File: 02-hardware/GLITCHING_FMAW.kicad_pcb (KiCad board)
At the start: 4 copper layers, 49 x 49 mm, 72 parts, among them J1 USB_C_Receptacle_USB2.0_16P, J2 AIN, J3 GLITCH, J4 ANA1, J5 ANA2, J6 ANA3, J7 GND, Q2 IRLB8721PBF, U1 TLV76133, U2 TLV76133, U3 LM358, U4 RP2040, U5 W25Q128JVS, U6 MS9280, Y1 12MHz

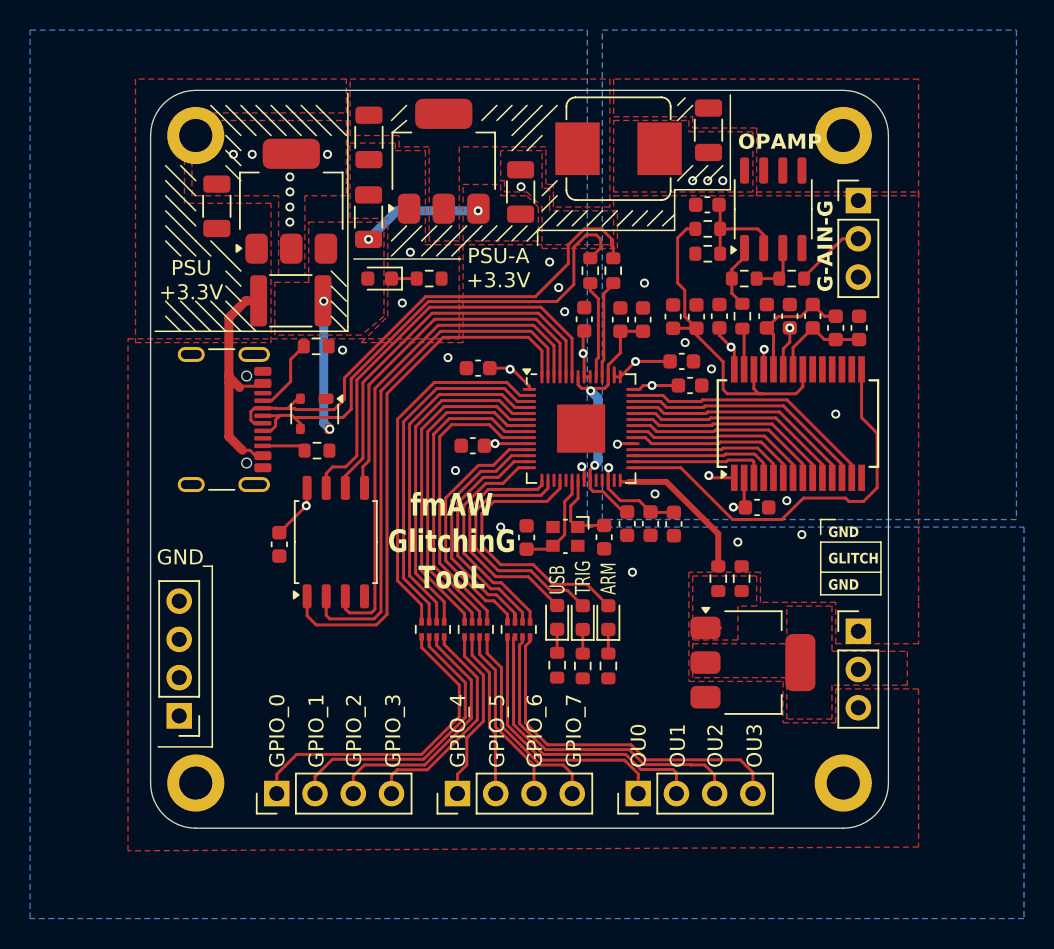
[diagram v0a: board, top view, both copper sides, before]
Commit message: update hw to mosfet | update expamples
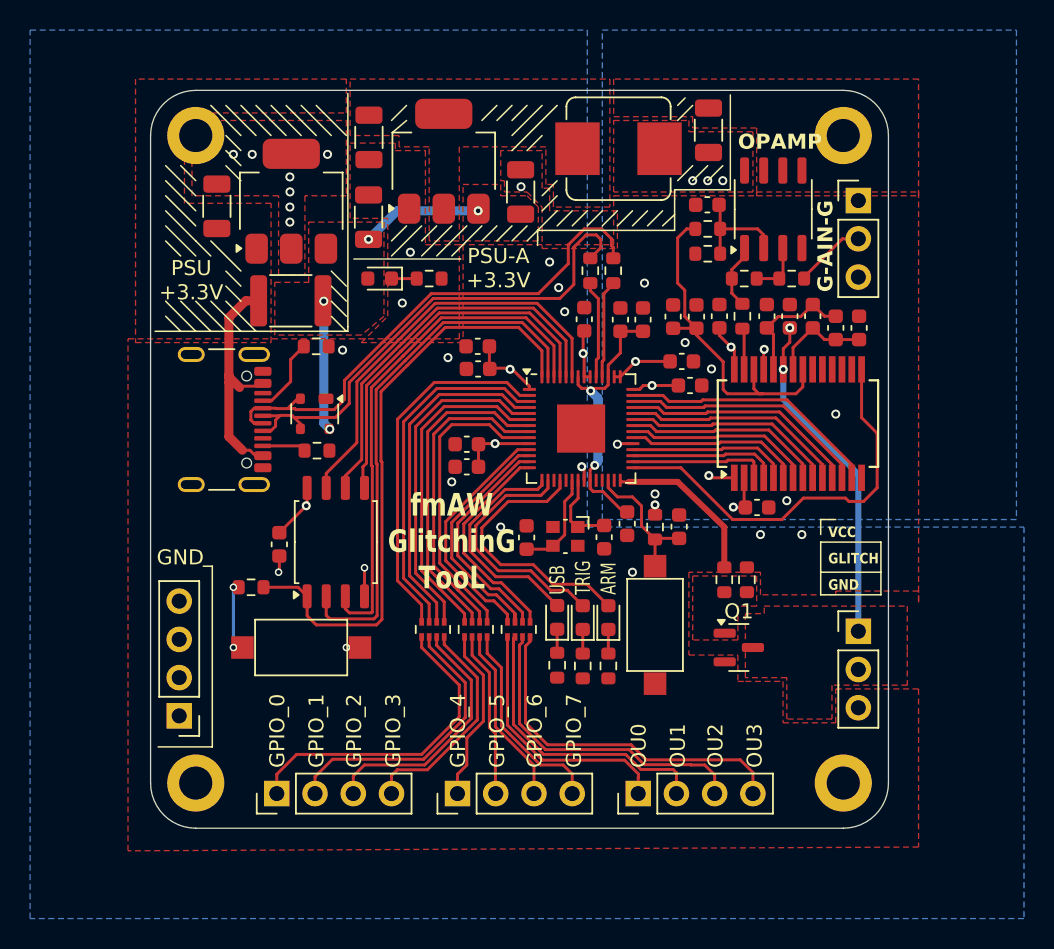
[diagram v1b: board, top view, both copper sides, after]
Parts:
- removed Q2: IRLB8721PBF, Package_TO_SOT_SMD:SOT-223-3_TabPin2
- added BOOT1: SW_DIP_x01, Button_Switch_SMD:SW_SPST_CK_RS282G05A3, F.Cu at (40.0, 61.0)
- added C29: 100nF, Capacitor_SMD:C_0603_1608Metric, F.Cu at (65.1, 53.0)
- added Q1: AO3400A, Package_TO_SOT_SMD:SOT-23, F.Cu at (69.1, 61.0)
- added R15: 1k, Resistor_SMD:R_0603_1608Metric, F.Cu at (36.7, 57.0)
- added R16: 1k, Resistor_SMD:R_0603_1608Metric, F.Cu at (63.5, 53.0)
- added RST1: SW_DIP_x01, Button_Switch_SMD:SW_SPST_CK_RS282G05A3, F.Cu at (63.5, 59.5)
- C17, C18: value tbd -> 8pF
- moved C19 17.6 mm to (51.7, 41.0), turned to 180 degrees
- moved C20 12.8 mm to (51.0, 49.0), turned to 180 degrees
- moved C25 0.41 mm to (51.0, 47.5)
- moved R10 0.41 mm to (68.1, 56.5)
- moved R11 0.36 mm to (69.6, 56.5)
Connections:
- J3 pad 1: GND -> +3.3VA
- U4 pad 26: +3.3V -> Net-(U4-RUN)
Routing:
- net +3.3VA: track 6.45 -> 25.9 mm, vias 5 -> 6
- net Net-(U4-RUN): track 0.00 -> 9.21 mm
- net Net-(BOOT1-Pad1): track 0.00 -> 5.05 mm, vias 0 -> 2
- net /CS: track 35.7 -> 39.8 mm
- net GND: track 3.10 -> 7.09 mm, vias 21 -> 24
- net +3.3V: track 33.3 -> 30.3 mm
- net /IO8: track 17.1 -> 16.2 mm
- net /IO9: track 17.0 -> 16.1 mm
- net /IO10: track 15.9 -> 15.1 mm
- net /SD1: track 35.0 -> 35.7 mm
- net /IO11: track 15.3 -> 14.5 mm
- net /IO17: track 10.1 -> 10.8 mm
- net /IO12: track 15.9 -> 15.2 mm
- net /SD2: track 33.9 -> 34.6 mm
- net /DP: track 34.8 -> 34.2 mm
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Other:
- board text added: "VCC"
